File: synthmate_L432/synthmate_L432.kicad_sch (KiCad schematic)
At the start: 14 parts, among them J1 USB_C_synthmate, J2 DIN-5_180degree, J3 USB_C_connector_board, J4 DIN-5_180degree, SW1 RotaryEncoder_Switch, SW2 SW_Push, SW3 SW_Push, U1 STM32L432KCUx, U3 MIC5365-1.0YC5

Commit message: pin headers, led, usart1
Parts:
- added D1: LED, LED_SMD:LED_0805_2012Metric_Pad1.15x1.40mm_HandSolder, symbol Device:LED
- added J5: Conn_01x16, symbol Connector_Generic:Conn_01x16
- added J6: Conn_01x13, symbol Connector_Generic:Conn_01x13
- added R4: 1k, symbol Device:R
- J3: footprint (none) -> Connector_USB:USB_C_Receptacle_GCT_USB4105-xx-A_16P_TopMnt_Horizontal
- SW1: footprint C41381718 -> Rotary_Encoder:RotaryEncoder_Bourns_Vertical_PEC12R-3x17F-Sxxxx
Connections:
- net 3V3: now also J6.1 (Pin_1)
- net BOOT0: now also J5.5 (Pin_5), J6.2 (Pin_2)
- net GND: now also D1.1 (K), J6.13 (Pin_13)
- net LPUART_RX: now also J5.4 (Pin_4)
- net LPUART_TX: now also J5.3 (Pin_3)
- net NRST: now also J6.3 (Pin_3)
- net USB_DM: now also J5.12 (Pin_12)
- net USB_DP: now also J5.13 (Pin_13)
- net enc_A: now also J5.1 (Pin_1)
- net enc_B: now also J5.2 (Pin_2)
- net pushbutton_A: now also J5.6 (Pin_6)
- net pushbutton_B: now also J5.7 (Pin_7)
- net PA7: now reaches U1.13 (PA7)
- net PA7: now also J5.8 (Pin_8)
- net PB0: now reaches U1.14 (PB0)
- net PB0: now also J6.6 (Pin_6)
- net PB1: now reaches U1.15 (PB1)
- net PB1: now also J6.7 (Pin_7)
- net LED: now reaches U1.18 (PA8)
- net LED: now also J5.9 (Pin_9), R4.1
- net USART1_TX: now reaches U1.19 (PA9)
- net USART1_TX: now also J5.10 (Pin_10)
- net PC14: now reaches U1.2 (PC14)
- net PC14: now also J6.4 (Pin_4)
- net USART1_RX: now reaches U1.20 (PA10)
- net USART1_RX: now also J5.11 (Pin_11)
- net PA13: now reaches U1.23 (PA13)
- net PA13: now also J5.14 (Pin_14)
- net PA14: now reaches U1.24 (PA14)
- net PA14: now also J5.15 (Pin_15)
- net PA15: now reaches U1.25 (PA15)
- net PA15: now also J5.16 (Pin_16)
- net PB3: now reaches U1.26 (PB3)
- net PB3: now also J6.8 (Pin_8)
- net PB4: now reaches U1.27 (PB4)
- net PB4: now also J6.9 (Pin_9)
- net PB5: now reaches U1.28 (PB5)
- net PB5: now also J6.10 (Pin_10)
- net PB6: now reaches U1.29 (PB6)
- net PB6: now also J6.11 (Pin_11)
- net PC15: now reaches U1.3 (PC15)
- net PC15: now also J6.5 (Pin_5)
- net PB7: now reaches U1.30 (PB7)
- net PB7: now also J6.12 (Pin_12)
- new net: D1.2 (A), R4.2
- no-connect marks 1 -> 8
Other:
- note added: "alternative TPS7A02 which CAPS?"
- note removed: "alternative TPS7A02"
- moved on the sheet: C1, C2, J1, J2, J3, J4, R1, R2, R3, SW1, SW2, SW3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

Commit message: pcb_v1
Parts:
- added C3, C4: 1uF, Capacitor_SMD:C_1206_3216Metric, symbol Device:C_Polarized
- added C5: 100nF, Capacitor_SMD:C_1206_3216Metric, symbol Device:C_Polarized
- added J7: Conn_01x04, Connector_PinSocket_2.54mm:PinSocket_1x04_P2.54mm_Vertical, symbol Connector_Generic:Conn_01x04
- added R5: 10k, Resistor_SMD:R_0805_2012Metric_Pad1.20x1.40mm_HandSolder, symbol Device:R
- added U2, U4: USBLC6-2SC6, Package_TO_SOT_SMD:SOT-23-6, symbol Power_Protection:USBLC6-2SC6
- C1: value 16V/47uF Tantalum -> 16V/47uF
- J1: footprint (none) -> Connector_USB:USB_C_Receptacle_GCT_USB4105-xx-A_16P_TopMnt_Horizontal
- J5: footprint (none) -> Connector_PinSocket_2.54mm:PinSocket_1x15_P2.54mm_Vertical
- J6: footprint (none) -> Connector_PinSocket_2.54mm:PinSocket_1x13_P2.54mm_Vertical
- R1, R2, R3, R4: footprint (none) -> Resistor_SMD:R_0805_2012Metric_Pad1.20x1.40mm_HandSolder
- SW2, SW3: footprint (none) -> Button_Switch_THT:SW_TH_Tactile_Omron_B3F-10xx
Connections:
- net 3V3: now also C4.1, C5.1, R5.2, U4.5 (VBUS)
- net 5V: now also C3.1, U2.5 (VBUS); no longer J3.A4 (VBUS), J3.A9 (VBUS), J3.B4 (VBUS), J3.B9 (VBUS)
- net GND: now also C3.2, C4.2, C5.2, U2.2 (GND), U4.2 (GND); no longer J3.A1 (GND), J3.A12 (GND), J3.B1 (GND), J3.B12 (GND), J3.S1 (SHIELD)
- net LPUART_RX: now also U4.1 (I/O1); no longer J1.A8 (SBU1), J3.A8 (SBU1)
- net LPUART_TX: now also U4.3 (I/O2); no longer J1.B8 (SBU2), J3.B8 (SBU2)
- net NRST: now also R5.1
- net USB_DM: now also U2.1 (I/O1); no longer J1.A7 (D-), J1.B7 (D-)
- net USB_DP: now also U2.3 (I/O2); no longer J1.A6 (D+), J1.B6 (D+)
- new net: J1.A6 (D+), J1.B6 (D+), U2.4 (I/O2)
- new net: J1.A7 (D-), J1.B7 (D-), U2.6 (I/O1)
- new net: J1.A8 (SBU1), U4.6 (I/O1)
- new net: J1.B8 (SBU2), U4.4 (I/O2)
- new net adaptor_5V: J3.A4 (VBUS), J3.A9 (VBUS), J3.B4 (VBUS), J3.B9 (VBUS), J7.1 (Pin_1)
- new net adaptor_GND: J3.A1 (GND), J3.A12 (GND), J3.B1 (GND), J3.B12 (GND), J3.S1 (SHIELD), J7.4 (Pin_4)
- new net adaptor_LPUART_RX: J3.A8 (SBU1), J7.2 (Pin_2)
- new net adaptor_LPUART_TX: J3.B8 (SBU2), J7.3 (Pin_3)
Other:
- moved on the sheet: C1, C2, J1, J3, J5, R2, R3

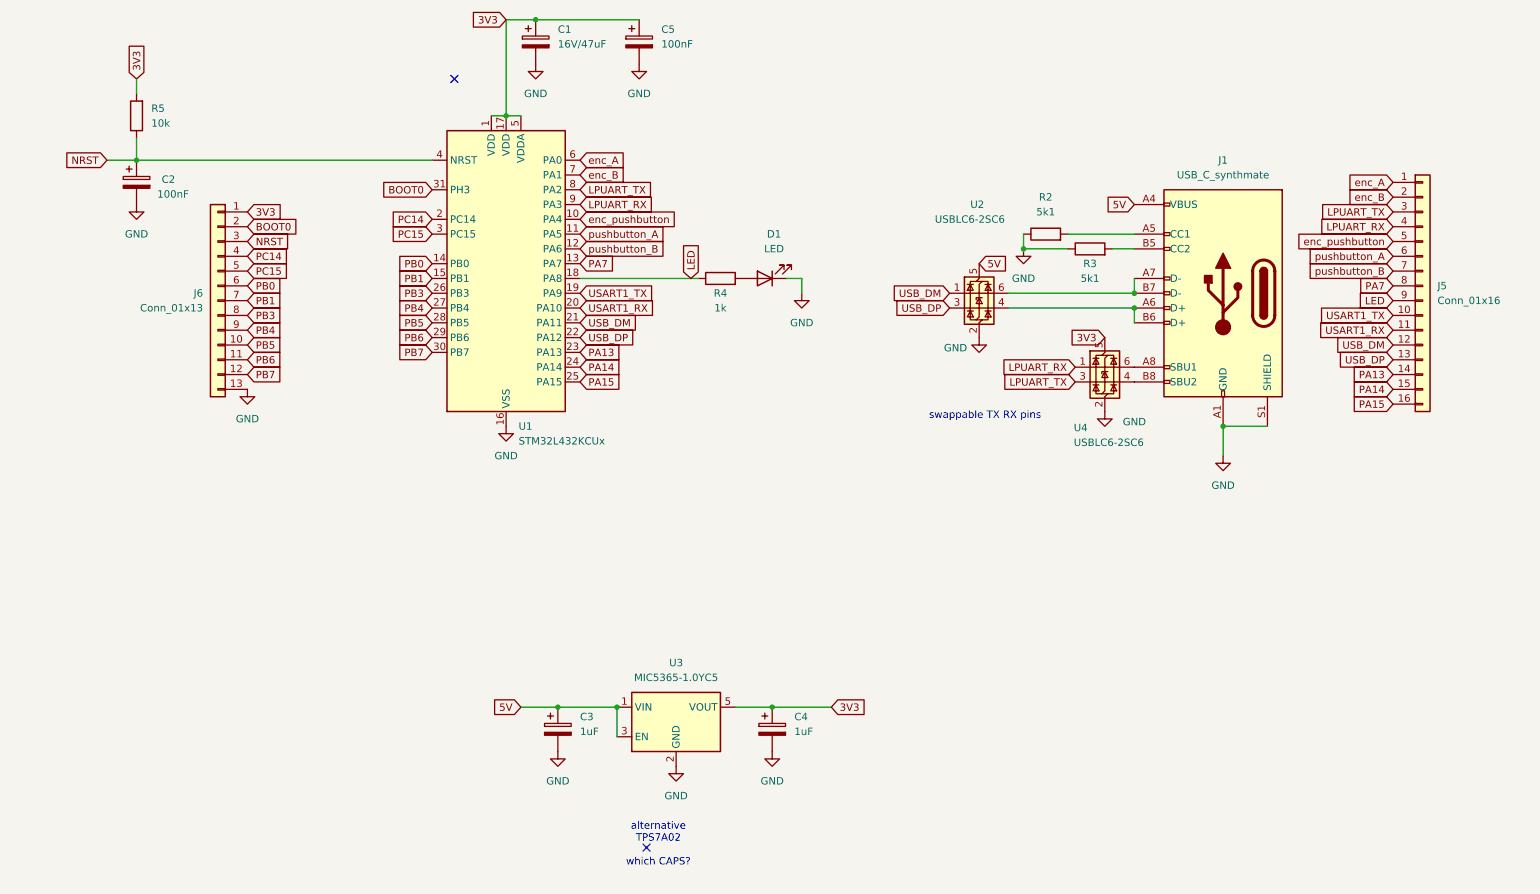
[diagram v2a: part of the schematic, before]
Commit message: switch to 4 layers, top layer signals routed
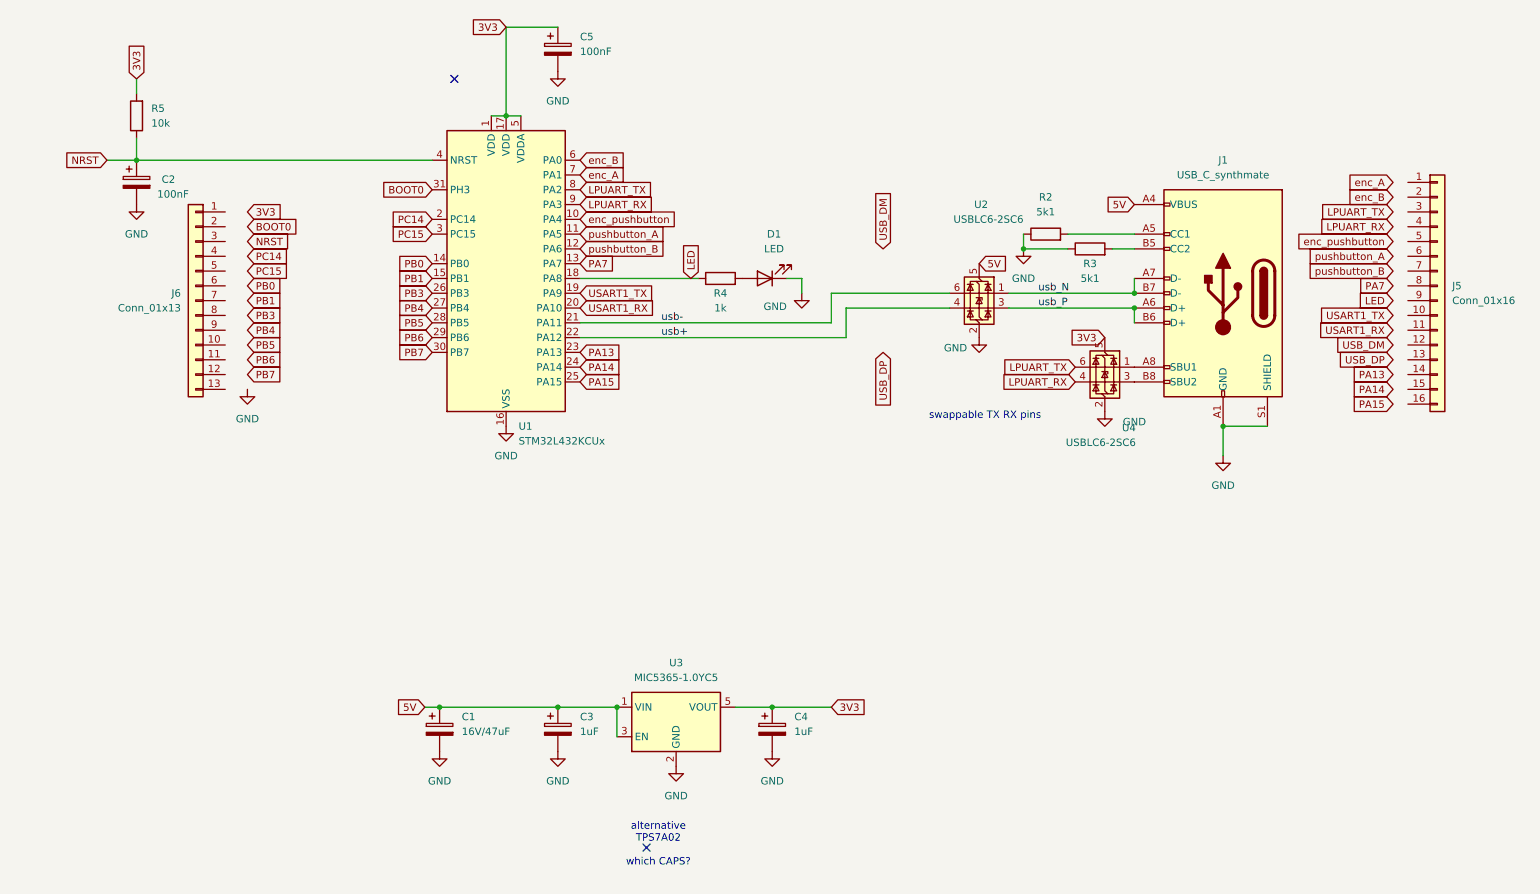
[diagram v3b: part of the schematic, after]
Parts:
- C2, C3, C4, C5: footprint Capacitor_SMD:C_1206_3216Metric -> Capacitor_SMD:C_0603_1608Metric_Pad1.08x0.95mm_HandSolder
- R1, R2, R3, R4, R5: footprint Resistor_SMD:R_0805_2012Metric_Pad1.20x1.40mm_HandSolder -> Resistor_SMD:R_0603_1608Metric_Pad0.98x0.95mm_HandSolder
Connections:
- net 3V3: no longer C1.1, J6.1 (Pin_1)
- net 5V: now also C1.1
- net BOOT0: no longer J5.5 (Pin_5), J6.2 (Pin_2)
- net GND: no longer J6.13 (Pin_13)
- net LED: no longer J5.9 (Pin_9)
- net LPUART_RX: now also U4.4 (I/O2); no longer J5.4 (Pin_4), U4.1 (I/O1)
- net LPUART_TX: now also U4.6 (I/O1); no longer J5.3 (Pin_3), U4.3 (I/O2)
- net NRST: no longer J6.3 (Pin_3)
- net PA13: no longer J5.14 (Pin_14)
- net PA14: no longer J5.15 (Pin_15)
- net PA15: no longer J5.16 (Pin_16)
- net PA7: no longer J5.8 (Pin_8)
- net PB0: no longer J6.6 (Pin_6)
- net PB1: no longer J6.7 (Pin_7)
- net PB3: no longer J6.8 (Pin_8)
- net PB4: no longer J6.9 (Pin_9)
- net PB5: no longer J6.10 (Pin_10)
- net PB6: no longer J6.11 (Pin_11)
- net PB7: no longer J6.12 (Pin_12)
- net PC14: no longer J6.4 (Pin_4)
- net PC15: no longer J6.5 (Pin_5)
- net USART1_RX: no longer J5.11 (Pin_11)
- net USART1_TX: no longer J5.10 (Pin_10)
- net USB_DM: no longer J5.12 (Pin_12), U1.21 (PA11), U2.1 (I/O1)
- net USB_DP: no longer J5.13 (Pin_13), U1.22 (PA12), U2.3 (I/O2)
- net enc_A: now also U1.7 (PA1); no longer J5.1 (Pin_1), U1.6 (PA0)
- net enc_B: now also U1.6 (PA0); no longer J5.2 (Pin_2), U1.7 (PA1)
- net pushbutton_A: no longer J5.6 (Pin_6)
- net pushbutton_B: no longer J5.7 (Pin_7)
- net usb_P: now reaches J1.A6 (D+), J1.B6 (D+)
- net usb_P: now also U2.3 (I/O2); no longer U2.4 (I/O2)
- net usb_N: now reaches J1.A7 (D-), J1.B7 (D-)
- net usb_N: now also U2.1 (I/O1); no longer U2.6 (I/O1)
- net at J1.A8 (SBU1): now also U4.1 (I/O1); no longer U4.6 (I/O1)
- net at J1.B8 (SBU2): now also U4.3 (I/O2); no longer U4.4 (I/O2)
- new net usb+: U1.22 (PA12), U2.4 (I/O2)
- new net usb-: U1.21 (PA11), U2.6 (I/O1)
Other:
- moved on the sheet: C1, C5, J5, J6

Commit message: added debounce
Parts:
- added C10, C6, C7, C8, C9: 100nF, Capacitor_SMD:C_0603_1608Metric_Pad1.08x0.95mm_HandSolder, symbol Device:C_Polarized
- added J8: Conn_ST_STDC14, symbol Connector:Conn_ST_STDC14
- added R10, R11, R12, R13, R14, R6, R7, R8, R9: 10k, Resistor_SMD:R_0603_1608Metric_Pad0.98x0.95mm_HandSolder, symbol Device:R
- added U5: 40106, Package_SO:TSSOP-14_4.4x5mm_P0.65mm, symbol 4xxx:40106
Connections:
- net 3V3: now also SW1.S2, R10.2, R11.2, R6.2, R7.2, U5.14 (VDD); no longer SW1.S1
- net BOOT0: now also U5.6; no longer R1.2, SW1.S2
- net GND: now also C10.2, C6.2, C7.2, C8.2, C9.2, U5.7 (VSS)
- net enc_A: now also U5.2; no longer SW1.A
- net enc_B: now also U5.4; no longer SW1.B
- net pushbutton_A: now also U5.8; no longer SW2.2
- net pushbutton_B: now also U5.10; no longer SW3.2
- new net: C9.1, R11.1, R13.1, SW3.2
- new net: R13.2, U5.11
- new net: R14.1, U5.5
- new net: C10.1, R1.2, R14.2, SW1.S1
- new net: C6.1, R7.1, R8.2, SW1.A
- new net: C8.1, R10.1, R12.1, SW2.2
- new net: R12.2, U5.9
- new net: R9.1, U5.3
- new net: R8.1, U5.1
- new net: C7.1, R6.1, R9.2, SW1.B
- new net: J8.5 (GND), J8.7 (GND)
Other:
- moved on the sheet: C1, C2, C3, C4, C5, D1, J1, J5, J6, R1, R2, R3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
